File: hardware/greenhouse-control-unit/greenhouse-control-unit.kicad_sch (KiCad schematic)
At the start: 53 parts, among them J1 Conn_01x01_Male, J10 Conn_ESP32_DevKitV1_Female, J12 Conn_01x05_Female, J13 Beep_Jumper, J15 Conn_01x05_Female, J16 Conn_01x05_Female, J2 Conn_01x01_Male, J3 Conn_01x01_Male, J4 Conn_01x01_Male, J5 Molex_KK-396_01x02, J6 Molex_KK-396_01x02, J7 Molex_KK-396_01x12, J8 Molex_KK-254_01x12, J9 Conn_01x09, Q1 BC547, Q2 BC547, Q3 BC547, Q4 BC547, Q5 2N3906, Q7 BC337, Q8 BC337, U1 PCF8574

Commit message: Fixed annotation references
Somehow became different to PCB run
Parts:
- renumbered C2 to C1, C1 to C2, D3 to D2, D5 to D3, D7 to D5, D2 to D6, D6 to D7, J6 to J1, J12 to J11, J16 to J12, J7 to J13, J8 to J14, J5 to J2, J13 to J3, J1 to J4, J2 to J5, J3 to J6, J4 to J7, J9 to J8, J15 to J9, Q7 to Q3, Q3 to Q6, Q8 to Q7, R2 to R1, R6 to R10, R9 to R11, R8 to R12, R12 to R13, R17 to R15, R20 to R17, R10 to R2, R13 to R3, R3 to R4, R11 to R5, R4 to R6, R1 to R8, R5 to R9

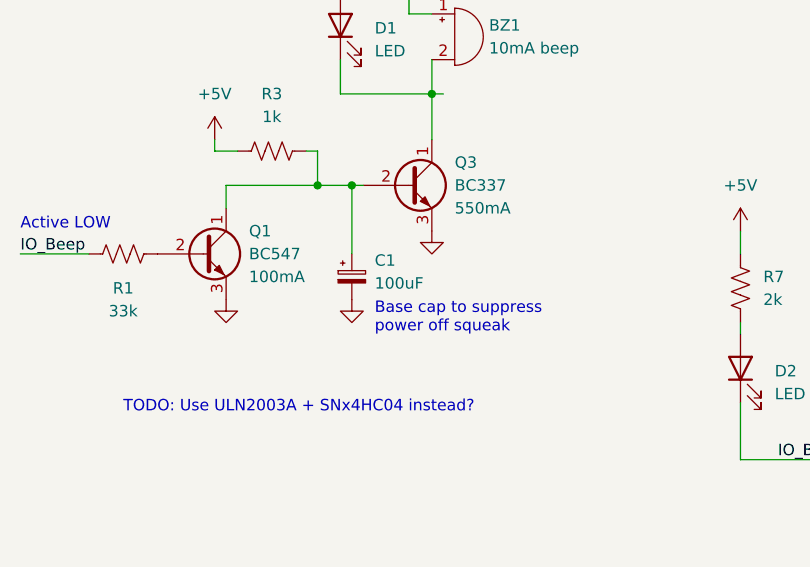
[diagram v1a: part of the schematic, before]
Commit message: Fixed beep pull-up cap value (pt2)
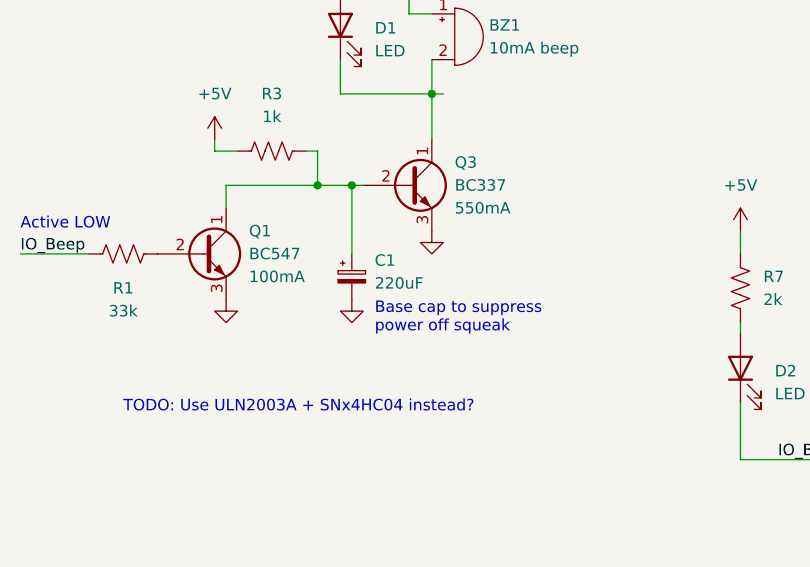
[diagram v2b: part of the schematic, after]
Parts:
- C1: value 100uF -> 220uF
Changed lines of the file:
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@@
       (effects (font (size 1.27 1.27)) (justify left))
     )
-    (property "Value" "100uF" (id 1) (at 166.37 259.8038 0)
+    (property "Value" "220uF" (id 1) (at 166.37 259.8038 0)
       (effects (font (size 1.27 1.27)) (justify left))
     )
@@
     )
     (path "/efe2628e-3c45-47e8-8d6b-7fc7f60ac03a"
-      (reference "C1") (unit 1) (value "100uF") (footprint "Capacitor_THT:CP_Radial_D6.3mm_P2.50mm")
+      (reference "C1") (unit 1) (value "220uF") (footprint "Capacitor_THT:CP_Radial_D6.3mm_P2.50mm")
     )
     (path "/3caa8576-ddd4-4b5f-ae0c-e72223d045f8"

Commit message: Add power in/out silkscreen text
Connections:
- net Batt+12V is gone; now on net +12V: J1.1 (Pin_1)
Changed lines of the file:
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@@
     (stroke (width 0) (type default) (color 0 0 0 0))
   )
-  (wire (pts (xy 165.1 68.58) (xy 175.26 68.58))
+  (wire (pts (xy 165.1 68.58) (xy 176.53 68.58))
     (stroke (width 0) (type default) (color 0 0 0 0))
   )
@@
   )
   (wire (pts (xy 439.42 201.93) (xy 449.58 201.93))
+    (stroke (width 0) (type default) (color 0 0 0 0))
+  )
+  (wire (pts (xy 176.53 67.31) (xy 176.53 68.58))
     (stroke (width 0) (type default) (color 0 0 0 0))
   )
@@
     )
     (property "Datasheet" "~" (id 3) (at 213.36 92.71 0)
+      (effects (font (size 1.27 1.27)) hide)
+    )
+    (pin "1")
+  )
+  (symbol (lib_id "power:+12V") (at 176.53 67.31 0) (unit 1)
+    (in_bom yes) (on_board yes) (fields_autoplaced)
+    (property "Reference" "#PWR?" (id 0) (at 176.53 71.12 0)
+      (effects (font (size 1.27 1.27)) hide)
+    )
+    (property "Value" "+12V" (id 1) (at 176.53 62.23 0))
+    (property "Footprint" "" (id 2) (at 176.53 67.31 0)
+      (effects (font (size 1.27 1.27)) hide)
+    )
+    (property "Datasheet" "" (id 3) (at 176.53 67.31 0)
       (effects (font (size 1.27 1.27)) hide)
     )
@@
       (reference "#PWR040") (unit 1) (value "+5V") (footprint "")
     )
+    (path "/52ee8d38-1ad7-4cb6-8628-555487f70804"
+      (reference "#PWR?") (unit 1) (value "+12V") (footprint "")
+    )
     (path "/d41bca08-cb1c-4470-aff5-bcac03d1a47a"

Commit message: Fixed missing GND on MCU
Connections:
- net GND: now also J10.17 (GND), J10.2 (GND)
- no-connect marks 32 -> 30

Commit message: Power saving when battery d/c
- Using FET to turn voltage divider off
- Also added light switch
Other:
- note added: "Design flaw: Even when PSU AC is d/c, PSU+12V will draw 100mA from Batt+12V. Possible solution is back-to-back P-MOS: https://www.circuitlab.com/editor/#?id=54h9w3b4hb4x"
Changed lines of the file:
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@@
     (effects (font (size 2 2)) (justify left bottom))
+  )
+  (text "Design flaw: Even when PSU AC is d/c,\nPSU+12V will draw 100mA from Batt+12V.\nPossible solution is back-to-back P-MOS:\nhttps://www.circuitlab.com/editor/#?id=54h9w3b4hb4x"
+    (at 138.43 101.6 0)
+    (effects (font (size 1.27 1.27)) (justify left bottom))
   )
   (text "Active HIGH" (at 302.26 257.81 0)
@@
   )
   (symbol (lib_id "power:PWR_FLAG") (at 177.8 88.9 270) (unit 1)
-    (in_bom yes) (on_board yes) (fields_autoplaced)
+    (in_bom yes) (on_board yes)
     (property "Reference" "#FLG02" (id 0) (at 179.705 88.9 0)
       (effects (font (size 1.27 1.27)) hide)

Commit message: First pass at R4
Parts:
- removed C1: 220uF, Capacitor_THT:CP_Radial_D6.3mm_P2.50mm, symbol Device:C_Polarized_Small
- removed D4: LED, LED_THT:LED_D5.0mm, symbol Device:LED
- removed D5: FR107, Diode_THT:D_DO-41_SOD81_P7.62mm_Horizontal, symbol Device:D
- removed J4, J5, J6, J7: Conn_01x01_Male, Connector_Pin:Pin_D1.0mm_L10.0mm, symbol Connector:Conn_01x01_Male
- removed Q1, Q4: BC547, Package_TO_SOT_THT:TO-92_Inline, symbol Transistor_BJT:BC547
- removed Q3: BC337, Package_TO_SOT_THT:TO-92_Inline, symbol Transistor_BJT:BC337
- removed Q5: 2N3906, Package_TO_SOT_THT:TO-92_Inline, symbol Transistor_BJT:2N3906
- added C3: 10nF, Capacitor_THT:C_Disc_D4.7mm_W2.5mm_P5.00mm, symbol Device:C_Small
- added D4: D, Diode_THT:D_DO-41_SOD81_P7.62mm_Horizontal, symbol Device:D
- added D5: LED, LED_THT:LED_D5.0mm, symbol Device:LED
- added F1: Fuse, Fuse:Fuse_Blade_Mini_directSolder, symbol Device:Fuse
- added J15: Molex_KK-396_01x02, Connector_Molex:Molex_KK-396_A-41791-0002_1x02_P3.96mm_Vertical, symbol Connector:Conn_01x02_Male
- added J4: PV Buck, Nick:Buck_Module, symbol Connector:Conn_01x04_Male
- added J6: 5V Buck, Nick:Buck_Module, symbol Connector:Conn_01x04_Male
- added Q1, Q10, Q4: 2N7000, Package_TO_SOT_THT:TO-92_Inline, symbol Transistor_FET:2N7000
- added Q11, Q12, Q5, Q8, Q9: FDP7030BL, Package_TO_SOT_THT:TO-220-3_Horizontal_TabDown, symbol Device:Q_NMOS_GDS
- added Q13, Q15, Q17, Q18: 2N7002, Package_TO_SOT_SMD:SOT-23, symbol Transistor_FET:2N7002
- added Q14, Q16, Q19, Q20: STD30NF06LT4, Package_TO_SOT_SMD:TO-252-2, symbol Device:Q_NMOS_GDS
- added Q3: TN0702, Package_TO_SOT_THT:TO-92_Inline, symbol Device:Q_NMOS_SGD
- added R18: 0R1, Resistor_SMD:R_2512_6332Metric_Pad1.40x3.35mm_HandSolder, symbol Device:R_US
- added R19, R20, R21, R23, R26, R27, R29, R32, R33: 10k, Resistor_THT:R_Axial_DIN0207_L6.3mm_D2.5mm_P7.62mm_Horizontal, symbol Device:R_US
- added R22, R25, R28, R30, R31: 100k, Resistor_THT:R_Axial_DIN0207_L6.3mm_D2.5mm_P7.62mm_Horizontal, symbol Device:R_US
- added R24: 1M, Resistor_THT:R_Axial_DIN0207_L6.3mm_D2.5mm_P7.62mm_Horizontal, symbol Device:R_US
- added U2: PCF8574, Package_SO:SOIC-16W_7.5x10.3mm_P1.27mm, symbol Interface_Expansion:PCF8574
- added U3, U4: ZXCT1107, Package_TO_SOT_SMD:SOT-23, symbol Amplifier_Current:ZXCT1107
- J1: Label (none) -> Batt
- J2: Label (none) -> PSU
- J5: renamed from J13; value Molex_KK-396_01x12 -> Conn_01x08_Male; footprint Connector_Molex:Molex_KK-396_A-41791-0012_1x12_P3.96mm_Vertical -> Connector_Molex:Molex_KK-396_A-41791-0008_1x08_P3.96mm_Vertical; symbol Connector:Conn_01x12_Male -> Connector:Conn_01x08_Male
- R1: value 33k -> 100k
- R10: value 220k -> 100k
- R12: value 10k -> 0R1; footprint Resistor_THT:R_Axial_DIN0207_L6.3mm_D2.5mm_P7.62mm_Horizontal -> Resistor_SMD:R_2512_6332Metric_Pad1.40x3.35mm_HandSolder
- R3, R8: value 1k -> 10k
- U1: footprint Package_DIP:DIP-16_W7.62mm_Socket -> Package_SO:SOIC-16W_7.5x10.3mm_P1.27mm
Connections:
- net +12V: now also R18.2, R19.2, R23.2, R26.1, R27.1, R29.1, R32.1, R33.1, U4.2 (Vs-); no longer J1.1 (Pin_1), J2.1 (Pin_1), J5.11 (Pin_11), J5.9 (Pin_9), R12.1
- net +3V3: now also R1.2, R8.1, C3.1, R21.1, R22.1, R28.1, R30.1, R31.1, U2.1 (A0), U2.16 (VDD)
- net +5V: now also R3.2, J6.2 (Pin_2); no longer R3.1
- net GND: now also C3.2, D5.1 (K), J6.3 (Pin_3), J6.4 (Pin_4), Q1.1 (S), Q12.3 (S), Q13.2 (S), Q14.3 (S), Q15.2 (S), Q16.3 (S), Q17.2 (S), Q18.2 (S), Q19.3 (S), Q20.3 (S), Q3.1 (S), Q8.3 (S), U2.2 (A1), U2.3 (A2), U2.8 (VSS); no longer J1.2 (Pin_2), J14.7 (BattRelayNC_B), J2.2 (Pin_2), J5.10 (Pin_10), J5.12 (Pin_12), J5.2 (Pin_2), J5.4 (Pin_4), J5.6 (Pin_6), J5.8 (Pin_8)
- net I2C_SCL: now also U2.14 (SCL)
- net I2C_SDA: now also U2.15 (SDA)
- net IO_Batt_EN: now also U1.9 (P4), Q10.1 (S); no longer R8.1, U1.4 (P0)
- net IO_BatteryLed: now also U1.7 (P3); no longer U1.9 (P4)
- net IO_Beep: now also U1.5 (P1), Q1.2 (G); no longer U1.6 (P2)
- net IO_CaseFan_EN: now also U1.4 (P0); no longer U1.7 (P3)
- net IO_PsuLed: now also U1.6 (P2); no longer U1.10 (P5)
- net at R8.2: now also Q4.2 (G)
- net IO_AC_EN: now reaches U1.11 (P6)
- net IO_AC_EN: now also R2.1
- net PV_Buck_Vcc: now reaches R12.2
- net PV_Buck_Vcc: now also J4.2 (Pin_2), U3.1 (Vs+)
- net PV_PWM: now reaches J10.10 (D32)
- net PV_PWM: now also Q11.1 (G), R20.2
- net PV_VS: now reaches J10.11 (D35)
- net PV_VS: now also R24.2, R25.1
- net PV_IS: now reaches J10.8 (D25)
- net PV_IS: now also U3.3 (OUT)
- net Common_IS: now reaches J10.9 (D33)
- net Common_IS: now also U4.3 (OUT)
- net at BZ1.2 (+), D1.1 (K): now also Q3.3 (D)
- net BattRelayNC_A: no longer names the net of J14.6 (NC)
- net Buck+12V: no longer names the net of D6.1 (K)
- net Buck+12V: now also J6.1 (Pin_1)
- removed net IO_PsuRelay_EN: R2.1, U1.5 (P1)
- net RFM95_EN: no longer names the net of J8.3 (Pin_3)
- net VSense renamed Common_VS
- new net: Q15.3 (D), Q16.1 (G), R29.2
- new net: Q10.3 (D), Q12.1 (G), Q9.1 (G), R23.1
- new net: Q12.2 (D), Q9.2 (D)
- new net: Q17.3 (D), Q19.1 (G), R32.2
- new net: D4.1 (K), J4.1 (Pin_1)
- new net: Q13.3 (D), Q14.1 (G), R27.2
- new net: Q10.2 (G), R21.2
- new net: Q18.3 (D), Q20.1 (G), R33.2
- new net: Q4.3 (D), Q5.1 (G), Q8.1 (G), R19.1
- new net: Q5.2 (D), Q8.2 (D)
- new net: Q1.3 (D), Q3.2 (G), R3.1
- new net: D5.2 (A), R26.2
- new net Batt+12V: F1.1, J1.1 (Pin_1), R12.1, U3.2 (Vs-)
- new net Batt_GND: J1.2 (Pin_2), Q11.3 (S), Q9.3 (S)
- new net Common+12V: F1.2, J2.1 (Pin_1), R18.1, U4.1 (Vs+)
- new net IO_OUT_1: Q13.1 (G), R22.2, U2.4 (P0)
- new net IO_OUT_2: Q17.1 (G), R30.2, U2.5 (P1)
- new net IO_OUT_3: Q15.1 (G), R28.2, U2.6 (P2)
- new net IO_OUT_4: Q18.1 (G), R31.2, U2.7 (P3)
- new net IO_PSU_EN: Q4.1 (S), U1.10 (P5)
- new net OUT_1_GND: J5.2 (Pin_2), Q14.2 (D)
- new net OUT_2_GND: J5.4 (Pin_4), Q19.2 (D)
- new net OUT_3_GND: J5.6 (Pin_6), Q16.2 (D)
- new net OUT_4_GND: J5.8 (Pin_8), Q20.2 (D)
- new net PSU_GND: J2.2 (Pin_2), Q5.3 (S)
- new net PV_GND: J15.2 (Pin_2), J4.4 (Pin_4), Q11.2 (D), R20.1, R25.2
- new net PV_Vcc: D4.2 (A), J15.1 (Pin_1), R24.1
- no-connect marks 30 -> 32
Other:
- note added: "PCF8574 outputs are HIGH at power on"
- note added: "PSU 10V NC relay module is active HIGH. Relay module coil must be open at power on. IO is HIGH at power on. Relay module IN requires 1.7mA. Active LOW must be pulled to VCC to disable (0.5uA). Active HIGH can be pulled to only 3V to enable (80mA)."
- note added: "Solar charger"
- note added: "TODO: Is the voltage divider islated to PV when using a low side NMOS?"
- note added: "UI"
- note removed: "Base cap to suppress power off squeak"
- note removed: "Battery NC relay draws 125mA. Inline with battery VCC."
- note removed: "Design flaw: Even when PSU AC is d/c, PSU+12V will draw 100mA from Batt+12V. Possible solution is back-to-back P-MOS: https://www.circuitlab.com/editor/#?id=54h9w3b4hb4x"
- note removed: "Diagnostic"
- note removed: "LOW to d/c battery"
- note removed: "Outputs HIGH at power on"
- note removed: "PSU 10V NC relay module is active HIGH. Relay module coil must be open at power on. IO is HIGH at power on. NPN required to drive relay module; relay module IN requires only 1.7mA, but IO is a weak current source (best used as current sink). Active LOW must be pulled to VCC to disable (0.5uA). Active HIGH can be pulled to only 3V to enable (80mA)."
- note removed: "TODO: Use ULN2003A + SNx4HC04 instead?"
- moved on the sheet: BZ1, C2, D1, D2, D3, D6, D7, J1, J10, J11, J12, J2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

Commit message: Optimized power use and moved beeper
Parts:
- removed R21, R8: 10k, Resistor_THT:R_Axial_DIN0207_L6.3mm_D2.5mm_P7.62mm_Horizontal, symbol Device:R_US
- R27, R29, R32, R33: value 10k -> 100k
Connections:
- net +3V3: now also Q10.2 (G), Q4.2 (G)
- net at R6.2: now also J3.2 (Pin_2); no longer J3.1 (Pin_1)
- net at BZ1.1 (-): now also J3.3 (Pin_3); no longer J3.2 (Pin_2)
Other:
- note removed: "TODO: Is the voltage divider islated to PV when using a low side NMOS?"
- note removed: "TODO: Use ULN2003A instead?"
- moved on the sheet: J3

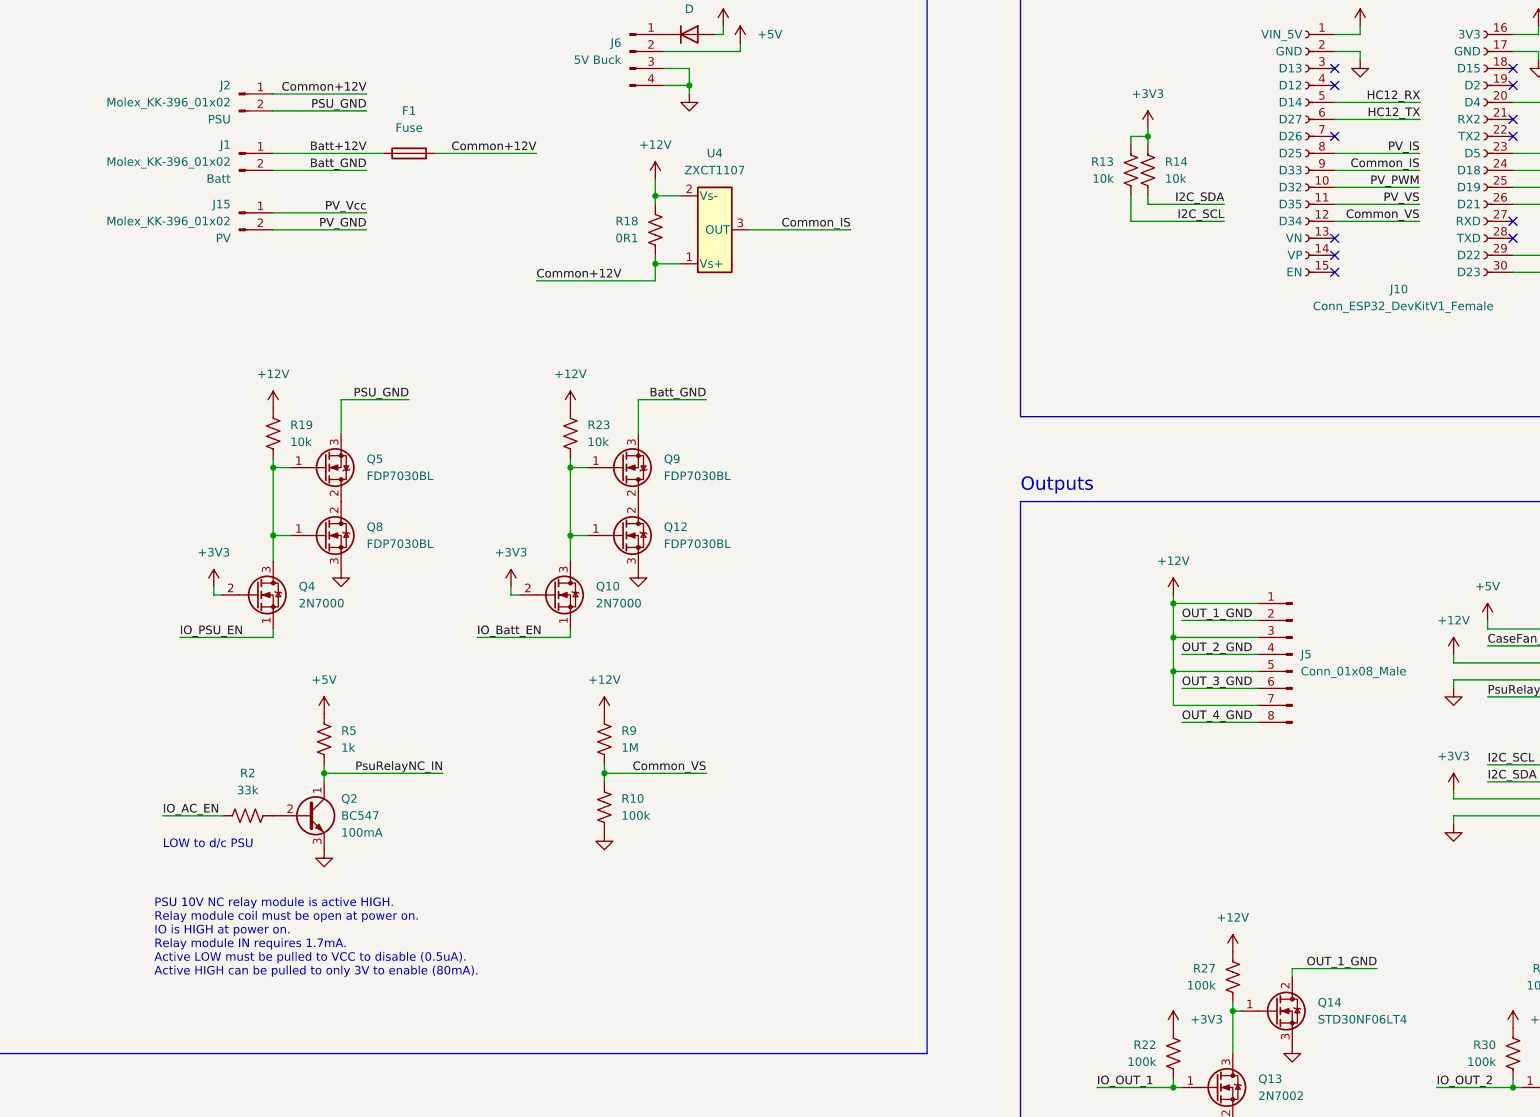
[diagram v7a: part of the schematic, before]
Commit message: Separate battery and PV voltage sensors
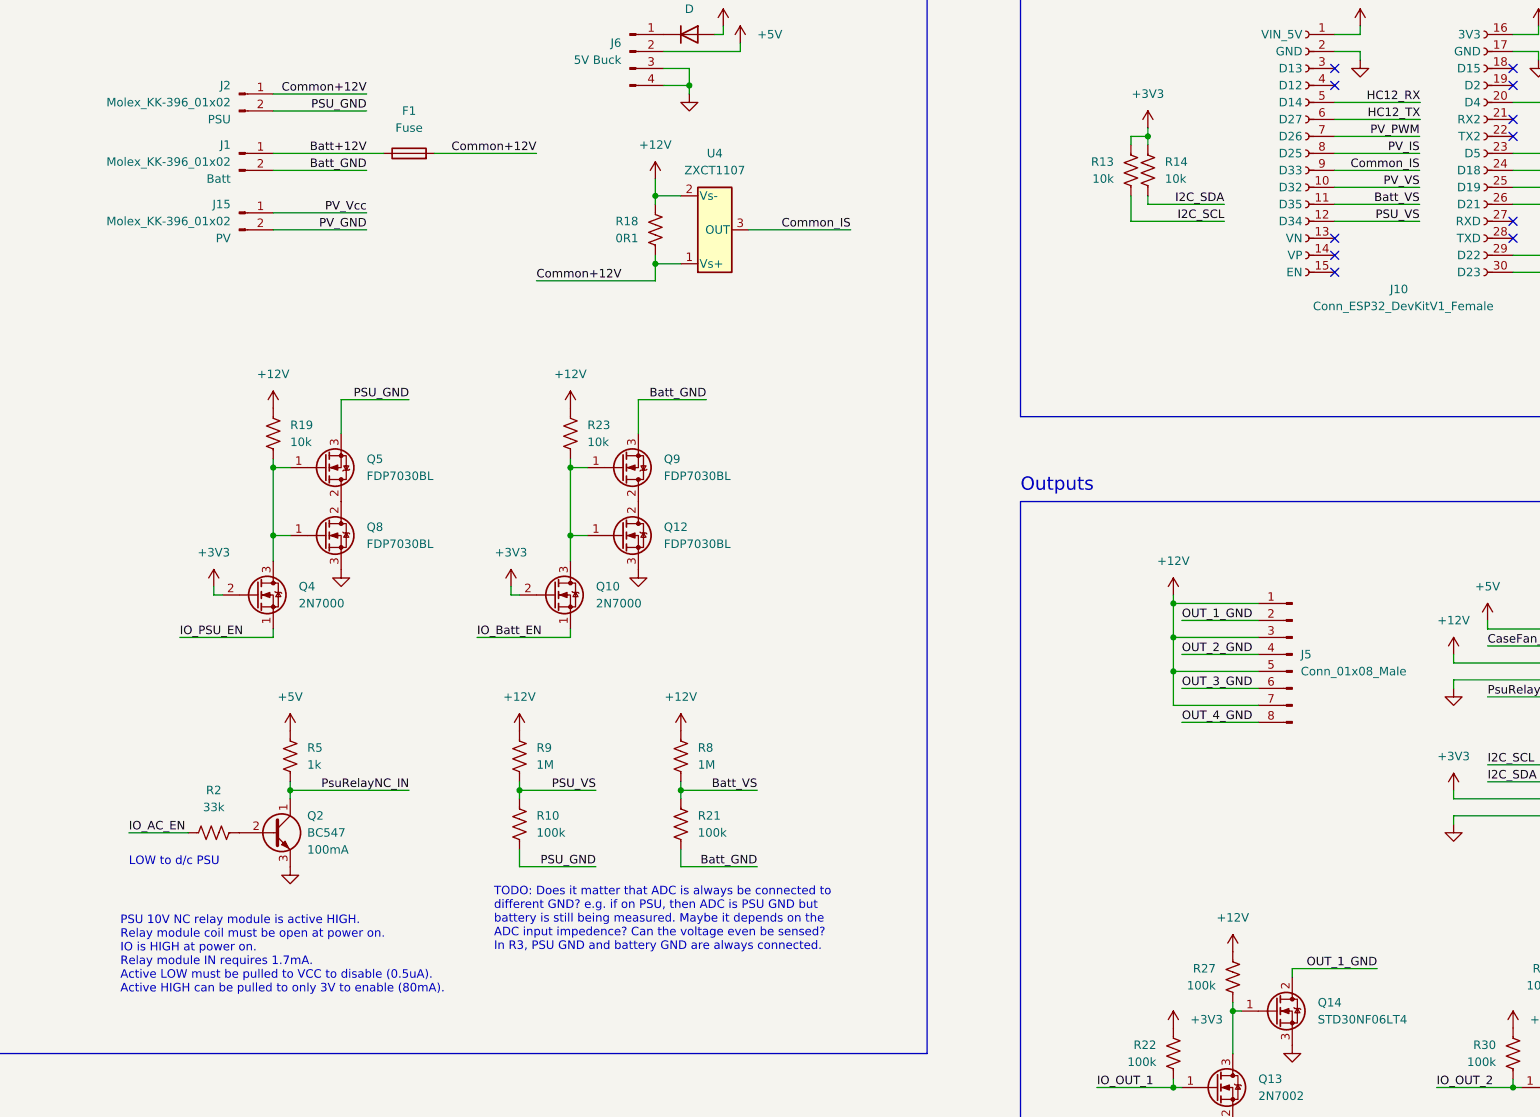
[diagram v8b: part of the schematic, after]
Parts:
- added R21: 100k, Resistor_THT:R_Axial_DIN0207_L6.3mm_D2.5mm_P7.62mm_Horizontal, symbol Device:R_US
- added R8: 1M, Resistor_THT:R_Axial_DIN0207_L6.3mm_D2.5mm_P7.62mm_Horizontal, symbol Device:R_US
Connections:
- net +12V: now also R8.1
- net Batt_GND: now also R21.2
- net GND: no longer R10.2
- net PSU_GND: now also R10.2
- net PV_PWM: now also J10.7 (D26); no longer J10.10 (D32)
- net PV_VS: now also J10.10 (D32); no longer J10.11 (D35)
- net Common_VS renamed PSU_VS
- new net Batt_VS: J10.11 (D35), R21.1, R8.2
- no-connect marks 32 -> 31
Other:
- note added: "TODO: Does it matter that ADC is always be connected to different GND? e.g. if on PSU, then ADC is PSU GND but battery is still being measured. Maybe it depends on the ADC input impedence? Can the voltage even be sensed? In R3, PSU GND and battery GND are always connected."
- moved on the sheet: Q2, R10, R2, R5, R9
